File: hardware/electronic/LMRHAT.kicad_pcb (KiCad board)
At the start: 2 copper layers, 58 x 93.6 mm, 63 parts, among them J1 Speaker Connector, J2 Serial, J3 PTT Button, J4 Top Controls, J5 RPi Expansion Connector, J8 Battery Connector, Q1 TSM850N06CX, Q3 TSM850N06CX, SW1 BTN_LEFT, SW2 BTN_UP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

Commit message: Connected power switch to a GPIO and moved the layout for readability
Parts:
- moved MK1 71.5 mm to (108.7, 41.6)
- moved R15 71.5 mm to (92.7, 63.8)
- moved C10 71.5 mm to (105.0, 112.9)
- moved C11 71.5 mm to (93.3, 126.1)
- moved C12 71.5 mm to (82.3, 125.9)
- moved C13 71.5 mm to (95.8, 106.7)
- moved C2 71.5 mm to (93.8, 85.2)
- moved C5 71.5 mm to (75.3, 116.7)
- moved C6 71.5 mm to (95.9, 58.7)
- moved C7 71.5 mm to (95.9, 61.2)
- moved C8 71.5 mm to (79.8, 40.3)
- moved C9 71.5 mm to (66.3, 123.1)
- moved J2 71.5 mm to (112.3, 48.4)
- moved J4 71.5 mm to (101.6, 40.1)
- moved J5 71.5 mm to (108.7, 89.3)
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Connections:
- J5 pad 22: Net-(J5-Pad22) -> SW_PWR
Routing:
- net SW_PWR: track 135.0 -> 199.5 mm, vias 0 -> 1

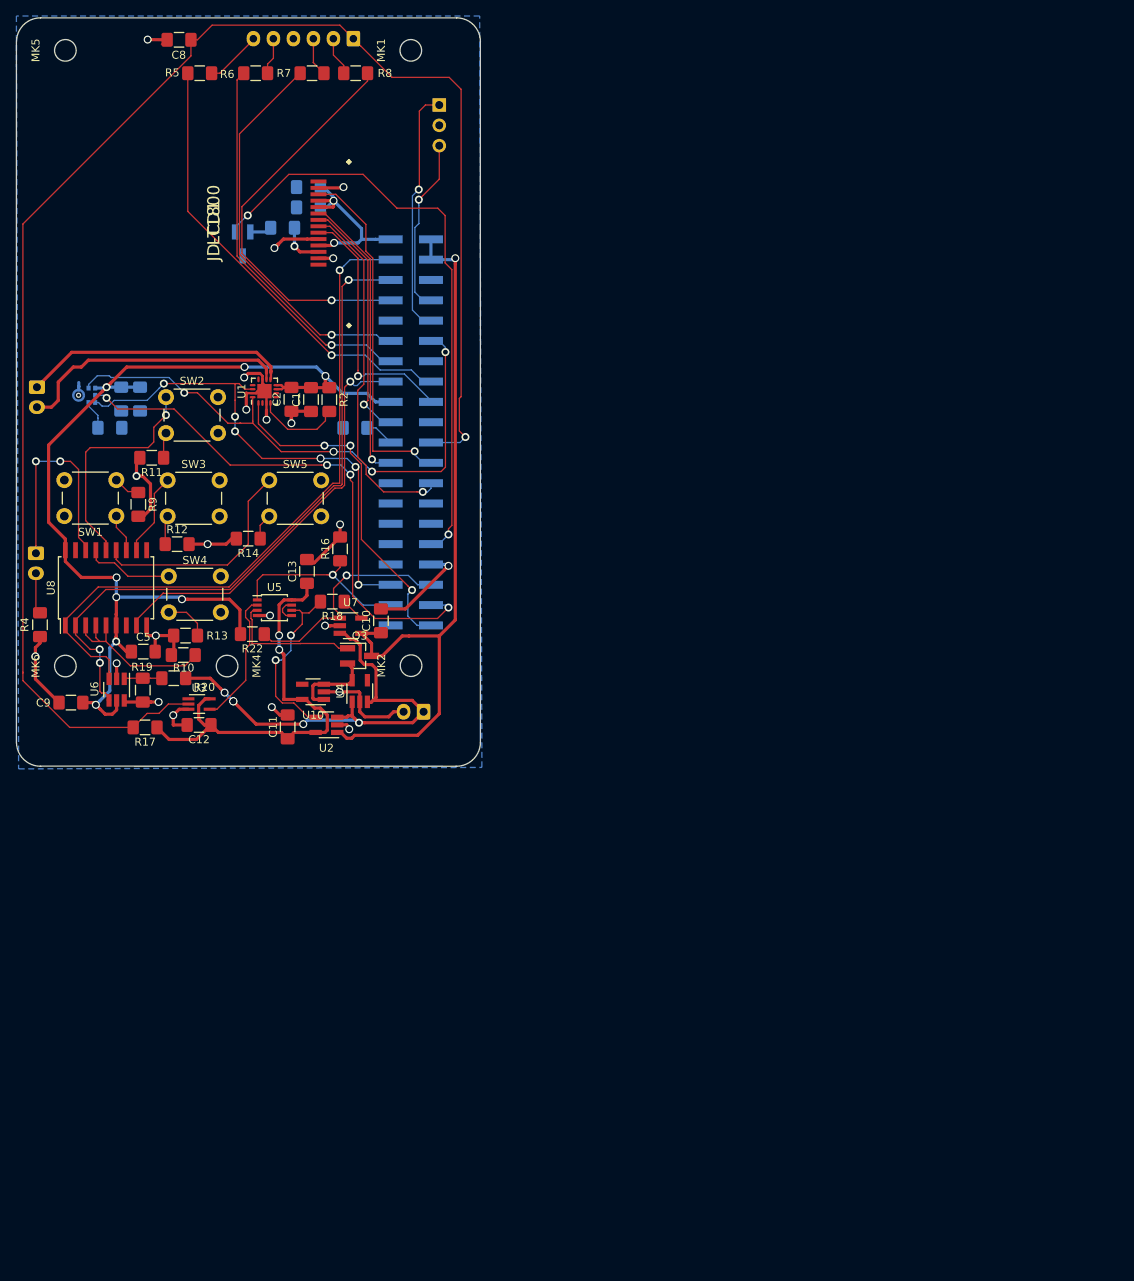
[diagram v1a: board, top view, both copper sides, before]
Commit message: Updated layout and schematic to match board dimensions of 50x80mm
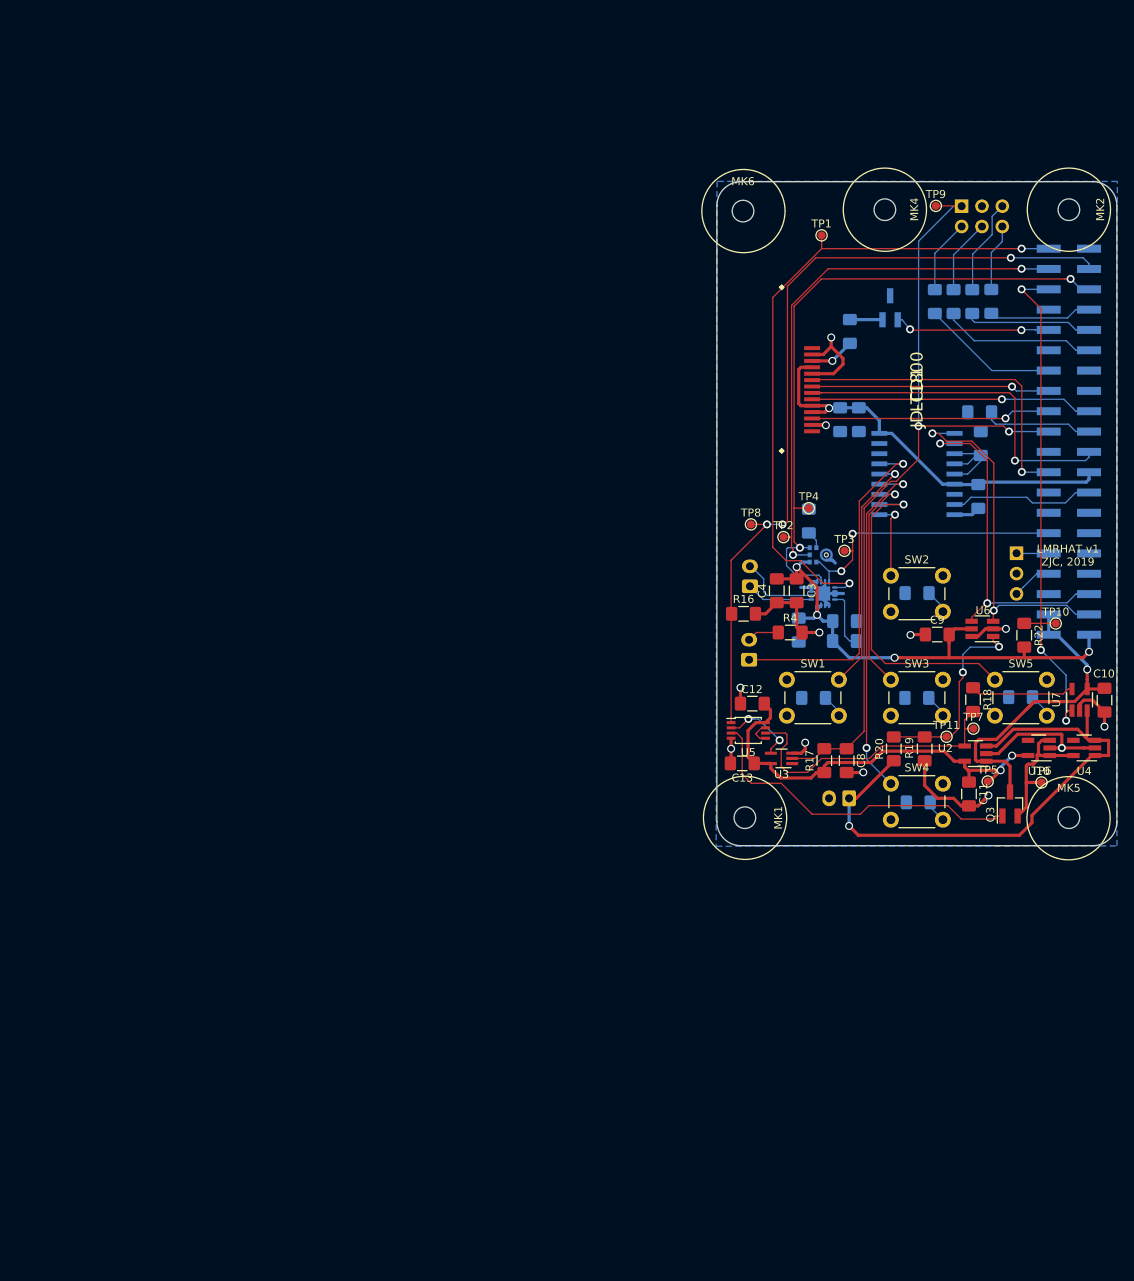
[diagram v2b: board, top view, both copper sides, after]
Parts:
- added TP1: , TestPoint:TestPoint_Pad_D1.0mm, F.Cu at (160.1, 64.7)
- added TP10: , TestPoint:TestPoint_Pad_D1.0mm, F.Cu at (189.4, 113.2)
- added TP11: , TestPoint:TestPoint_Pad_D1.0mm, F.Cu at (175.7, 127.4)
- added TP2: , TestPoint:TestPoint_Pad_D1.0mm, F.Cu at (155.3, 102.4)
- added TP3: , TestPoint:TestPoint_Pad_D1.0mm, F.Cu at (162.9, 104.1)
- added TP4: , TestPoint:TestPoint_Pad_D1.0mm, F.Cu at (158.5, 98.8)
- added TP5: , TestPoint:TestPoint_Pad_D1.0mm, F.Cu at (180.8, 133.0)
- added TP6: , TestPoint:TestPoint_Pad_D1.0mm, F.Cu at (187.6, 133.1)
- added TP7: , TestPoint:TestPoint_Pad_D1.0mm, F.Cu at (179.1, 126.4)
- added TP8: , TestPoint:TestPoint_Pad_D1.0mm, F.Cu at (151.3, 100.8)
- added TP9: , TestPoint:TestPoint_Pad_D1.0mm, F.Cu at (174.4, 61.0)
- C1, C2, C5, R10, R11, R12, R13, R14, R2, R5, R6, R7, R8, R9, U1, U8: moved to B.Cu
- C3, C4: moved to F.Cu
- J4: footprint Connector_JST:JST_EH_B06B-EH-A_1x06_P2.50mm_Vertical -> Connector_PinHeader_2.54mm:PinHeader_2x03_P2.54mm_Vertical
- SW1, SW2, SW3, SW4, SW5: footprint LMRHAT:SW_PUSH_6mm_SEP -> Button_Switch_THT:SW_PUSH_6mm_H5mm
- moved MK5 157.9 mm to (191.0, 137.5), turned to 0 degrees
- moved C8 122.8 mm to (163.2, 130.4), turned to 270 degrees
- moved C9 108.6 mm to (174.5, 114.6)
- moved U6 108.5 mm to (180.2, 113.9), turned to 180 degrees
- moved C5 106.2 mm to (179.7, 97.3), turned to 270 degrees
- moved MK1 104.6 mm to (150.5, 137.5), turned to 0 degrees
- moved R10 103.1 mm to (180.0, 90.7), turned to 90 degrees
- moved R5 103.0 mm to (181.3, 73.0), turned to 270 degrees
- moved U8 102.4 mm to (172.0, 94.5), turned to 180 degrees
- moved MK6 102.0 mm to (150.3, 61.7), turned to 0 degrees
- moved MK4 100.1 mm to (168.0, 61.5), turned to 0 degrees
- moved MK2 100.0 mm to (191.0, 61.5), turned to 0 degrees
- moved R14 98.6 mm to (185.0, 122.4)
- moved R19 98.0 mm to (173.0, 128.9)
- moved R11 97.2 mm to (172.0, 109.4)
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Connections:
- J4 pad 3: Net-(J4-Pad3) -> GND
- J4 pad 4: GND -> Net-(J4-Pad4)
- J5 pad 11: VOL_B -> Net-(J5-Pad11)
- J5 pad 13: CHAN_A -> Net-(J5-Pad13)
- J5 pad 16: CHAN_B -> Net-(J5-Pad16)
- J5 pad 28: Net-(J5-Pad28) -> VOL_A
- J5 pad 29: Net-(J5-Pad29) -> VOL_B
- J5 pad 31: Net-(J5-Pad31) -> CHAN_A
- J5 pad 33: Net-(J5-Pad33) -> CHAN_B
- J5 pad 7: VOL_A -> Net-(J5-Pad7)
- R7 pad 1: Net-(J4-Pad3) -> Net-(J4-Pad4)
- U1 pad 12: Net-(U1-Pad12) -> GND
- U1 pad 13: Net-(U1-Pad13) -> GND
- U1 pad 2: Net-(U1-Pad2) -> GND
- U1 pad 5: Net-(U1-Pad5) -> GND
- U1 pad 6: Net-(U1-Pad6) -> GND
- U8 pad 10: Net-(U8-Pad10) -> BTN_UP
- U8 pad 11: BTN_SELECT -> BTN_RIGHT
- U8 pad 12: BTN_LEFT -> BTN_SELECT
- U8 pad 13: BTN_RIGHT -> BTN_DOWN
- U8 pad 14: BTN_UP -> BTN_LEFT
- U8 pad 15: BTN_DOWN -> BTN_PTT
- U8 pad 16: BTN_PTT -> Net-(U8-Pad16)
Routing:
- net SW_PWR: track 199.5 -> 101.9 mm, vias 1 -> 2
- net PWR_STATUS: track 23.1 -> 101.6 mm, vias 1 -> 3
- net BKLIGHT: track 74.8 -> 20.1 mm
- net +5V: track 93.1 -> 42.1 mm
- net CHAN_B: track 56.5 -> 12.9 mm, vias 1 -> 0
- net SDA: track 84.7 -> 42.8 mm, vias 3 -> 2
- net +3V3: track 158.1 -> 116.9 mm, vias 10 -> 5
- net SCL: track 85.6 -> 44.4 mm, vias 1 -> 2
- net PCM_DOUT: track 43.4 -> 83.4 mm, vias 3 -> 2
- net BATT_CHARGE: track 28.4 -> 65.5 mm, vias 1 -> 3
- net PCM_CLK: track 71.4 -> 36.0 mm, vias 4 -> 2
- net INT_BTN: track 52.5 -> 18.0 mm, vias 1 -> 0
- net BTN_DOWN: track 10.9 -> 44.1 mm, vias 0 -> 2
- net VOL_A: track 50.0 -> 17.2 mm, vias 1 -> 0
- net CHAN_A: track 47.9 -> 15.9 mm, vias 1 -> 0
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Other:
- board size 58 x 93.6 mm -> 50 x 83 mm
- rule via_min_drill: 0.3 -> 0.3302
- rule via_min_size: 0.8 -> 0.6858
- board text added: "LMRHAT v1 ZJC, 2019"
